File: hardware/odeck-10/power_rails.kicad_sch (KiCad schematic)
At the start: 0 parts

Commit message: Draft power sheets (input, laptop output, rails) and BOM stock audit
- power_input: TPS26750/TPD4S480 EPR sink, LM74800 PD-in and barrel paths
  (reverse/OV/UV), hardware PD-in priority, EXT_PWR_PRESENT, INA237 VIN monitor
- power_laptop: LM51770 buck-boost 5-28 V x 5 A with VSEL-only voltage steps,
  gated source switch, interlocked bus-power sink, latched 30.8 V OVP, INA226
- power_rails: LM5148 5 V/8 A with ideal-diode backfeed blocking, TPS62933
  3.3 V and 1.15 V, INA226
- tools/bom_check.py: JLC-stock-only audit (>=5); all 116 parts pass
- schgen fixes: multi-line notes, PWR_FLAG skipped in verify, import --force
- docs: design notes per sheet, I2C map, cross-sheet integration items

Co-Authored-By: Claude Opus 5.5 <noreply@anthropic.com>
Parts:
- added C301: 47u/100V, Capacitor_SMD:CP_Elec_10x10, symbol Device:C_Polarized
- added C302, C303, C304, C305: 4.7u/100V, Capacitor_SMD:C_1210_3225Metric, symbol Device:C
- added C306, C307: 100n/100V, Capacitor_SMD:C_0603_1608Metric, symbol Device:C
- added C308, C318, C323, C329, C331, C337, C338: 100n, Capacitor_SMD:C_0402_1005Metric, symbol Device:C
- added C309: 1n/100V, Capacitor_SMD:C_0603_1608Metric, symbol Device:C
- added C310, C311, C312, C313, C314, C315: 47u/10V, Capacitor_SMD:C_1210_3225Metric, symbol Device:C
- added C316: 1u/100V, Capacitor_SMD:C_0805_2012Metric, symbol Device:C
- added C317: 4.7u, Capacitor_SMD:C_0603_1608Metric, symbol Device:C
- added C319: 10n, Capacitor_SMD:C_0402_1005Metric, symbol Device:C
- added C320: 100p, Capacitor_SMD:C_0402_1005Metric, symbol Device:C
- added C321, C322: 100n/50V, Capacitor_SMD:C_0603_1608Metric, symbol Device:C
- added C324: 330u/6.3V, Capacitor_SMD:CP_Elec_6.3x5.9, symbol Device:C_Polarized
- added C325, C326, C332, C333, C334: 22u, Capacitor_SMD:C_0805_2012Metric, symbol Device:C
- added C327, C328, C335, C336: 10u, Capacitor_SMD:C_0805_2012Metric, symbol Device:C
- added C330: 22n, Capacitor_SMD:C_0402_1005Metric, symbol Device:C
- added C339, C340, C341, C342: 22u, Capacitor_SMD:C_0603_1608Metric, symbol Device:C
- added D301: BAT46W, Diode_SMD:D_SOD-123, symbol Device:D_Schottky
- added L301: 4.7u, odeck:IND-SMD_L13.45-W12.6, symbol odeck:MWSA1206S-4R7MT
- added L302: 2.2u, odeck:IND-SMD_L5.4-W5.2, symbol odeck:MWSA0503S-2R2MT
- added L303: 1.5u, odeck:IND-SMD_L5.4-W5.2, symbol odeck:MWSA0503S-1R5MT
- added Q301: BSZ070N08LS5, odeck:PG-TSDSON-8_L3.3-W3.3-P0.65-BL-1, symbol odeck:BSZ070N08LS5
- added Q302: BSC0805LS, odeck:PG-TDSON-8_L5.2-W5.9-P1.27-LS6.2-BL-EP, symbol odeck:BSC0805LS
- added Q303: BSC0901NS, odeck:DFN-8_L5.9-W5.2-P1.27-LS6.2-BL, symbol odeck:BSC0901NS
- added R301: 0, Resistor_SMD:R_0402_1005Metric, symbol Device:R
- added R302: 2.2, Resistor_SMD:R_0805_2012Metric, symbol Device:R
- added R303: 4m, Resistor_SMD:R_2512_6332Metric, symbol Device:R
- added R304: 100k, Resistor_SMD:R_0805_2012Metric, symbol Device:R
- added R305: 14.3k, Resistor_SMD:R_0402_1005Metric, symbol Device:R
- added R306: 73.2k, Resistor_SMD:R_0402_1005Metric, symbol Device:R
- added R307: 41.2k, Resistor_SMD:R_0402_1005Metric, symbol Device:R
- added R308: 64.9k, Resistor_SMD:R_0402_1005Metric, symbol Device:R
- added R309, R317: 12k, Resistor_SMD:R_0402_1005Metric, symbol Device:R
- added R310, R316, R318, R321: 10k, Resistor_SMD:R_0402_1005Metric, symbol Device:R
- added R311, R313, R319: 100k, Resistor_SMD:R_0402_1005Metric, symbol Device:R
- added R312: 2m, Resistor_SMD:R_2512_6332Metric, symbol Device:R
- added R314: 39k, Resistor_SMD:R_0402_1005Metric, symbol Device:R
- added R315: 31.6k, Resistor_SMD:R_0402_1005Metric, symbol Device:R
- added R320: 4.42k, Resistor_SMD:R_0402_1005Metric, symbol Device:R
- added U301: LM5148, odeck:VQFN-24_L5.5-W3.5-P0.50-BL-EP-2, symbol odeck:LM5148RGYR
- added U302: LM74700-Q1, odeck:SOT-23-6_L2.9-W1.6-P0.95-LS2.8-TL, symbol odeck:LM74700QDBVTQ1
- added U303: INA226, odeck:MSOP-10_L3.0-W3.0-P0.50-LS5.0-BL, symbol odeck:INA226AIDGSR
- added U304: TPS62933, odeck:SOT-583-8_L2.1-W1.2-P0.50-LS1.6-BR, symbol odeck:TPS62933DRLR
- added U305: TPS62933P, odeck:SOT-583-8_L2.1-W1.2-P0.50-LS1.6-BL, symbol odeck:TPS62933PDRLR
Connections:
- new net +1V15: C339.1, C340.1, C341.1, C342.1, L303.2, R320.1
- new net +3V3: C323.1, C332.1, C333.1, C334.1, L302.2, R315.1, R317.1, R319.2, U303.2 (A0), U303.6 (VS+)
- new net +5V: C324.1, C325.1, C326.1, C327.1, C328.1, C329.1, C335.1, C336.1, C337.1, R312.2, R313.1, U303.8 (VBUS), U303.9 (VIN-), U304.3 (VIN), U305.3 (VIN)
- new net 1V15_BST: C338.1, U305.6 (BST)
- new net 1V15_EN: R317.2, R318.1, U305.2 (EN)
- new net 1V15_FB: R320.2, R321.1, U305.8 (FB)
- new net 1V15_SW: C338.2, L303.1, U305.5 (SW)
- new net 3V3_BST: C331.1, U304.6 (BST)
- new net 3V3_EN: R313.2, R314.1, U304.2 (EN)
- new net 3V3_FB: R315.2, R316.1, U304.8 (FB)
- new net 3V3_SS: C330.1, U304.7 (SS)
- new net 3V3_SW: C331.2, L302.1, U304.5 (SW)
- new net 5V_BOOT: C308.1, U301.15 (CBOOT)
- new net 5V_BUCK: C310.1, C311.1, C312.1, C313.1, C314.1, C315.1, C321.2, Q303.1 (S), Q303.2 (S), Q303.3 (S), R303.2, R308.1, R311.1, U301.16 (VCCX), U301.21 (VOUT), U302.3 (EN), U302.6 (ANODE)
- new net 5V_CC: C319.1, R310.2
- new net 5V_CNFG: R307.1, U301.3 (CNFG)
- new net 5V_COMP: C320.1, R310.1, U301.5 (EXTCOMP)
- new net 5V_EN: R304.2, R305.1, U301.19 (EN)
- new net 5V_FB: R308.2, R309.1, U301.6 (FB)
- new net 5V_HG: Q301.4 (G), R301.2
- new net 5V_HO: R301.1, U301.13 (HO)
- new net 5V_ISNS: L301.2, R303.1, U301.20 (ISNS+)
- new net 5V_LG: Q302.4 (G), U301.11 (LO)
- new net 5V_OR: C322.1, Q303.5 (D), Q303.6 (D), Q303.7 (D), Q303.8 (D), Q303.9 (D), R312.1, U302.4 (CATHODE), U303.10 (VIN+)
- new net 5V_ORG: Q303.4 (G), U302.5 (GATE)
- new net 5V_RT: R306.1, U301.4 (RT)
- new net 5V_SNB: C309.1, R302.2
- new net 5V_SW: C308.2, L301.1, Q301.1 (S), Q301.2 (S), Q301.3 (S), Q302.5 (D), Q302.6 (D), Q302.7 (D), Q302.8 (D), Q302.9 (EP), R302.1, U301.14 (SW)
- new net 5V_VCAP: C321.1, U302.1 (VCAP)
- new net 5V_VCC: C317.1, U301.9 (VCC)
- new net 5V_VDDA: C318.1, U301.18 (PFM/SYNC), U301.8 (VDDA)
- new net 5V_VINC: C316.1, D301.1 (K), U301.12 (VIN)
- new net GND: C301.2, C302.2, C303.2, C304.2, C305.2, C306.2, C307.2, C309.2, C310.2, C311.2, C312.2, C313.2, C314.2, C315.2, C316.2, C317.2, C318.2, C319.2, C320.2, C322.2, C323.2, C324.2, C325.2, C326.2, C327.2, C328.2, C329.2, C330.2, C332.2, C333.2, C334.2, C335.2, C336.2, C337.2, C339.2, C340.2, C341.2, C342.2, Q302.1 (S), Q302.2 (S), Q302.3 (S), R305.2, R306.2, R307.2, R309.2, R314.2, R316.2, R318.2, R321.2, U301.1 (NC), U301.10 (PGND), U301.2 (NC), U301.22 (NC), U301.23 (NC), U301.24 (NC), U301.25 (EP), U301.7 (AGND), U302.2 (GND), U303.1 (A1), U303.7 (GND), U304.1 (RT), U304.4 (GND), U305.1 (RT), U305.4 (GND)
- new net I2C_SYS_SCL: U303.5 (SCL)
- new net I2C_SYS_SDA: U303.4 (SDA)
- new net PG_5V: R311.2, U301.17 (PG/SYNCOUT)
- new net RAILS_PG: R319.1, U305.7 (PG)
- new net VIN: C301.1, C302.1, C303.1, C304.1, C305.1, C306.1, C307.1, D301.2 (A), Q301.5 (D), Q301.6 (D), Q301.7 (D), Q301.8 (D), R304.1
- no-connect marks 0 -> 1
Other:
- note added: "+1V1: not needed. RP2350 core (DVDD 1.1 V) comes from its internal switching regulator (VREG_VIN from +3V3)."
- note added: "+5V rises 5.0 -> 5.11 V, EXT_PWR_PRESENT opens the sink switch. Loss of VIN: +5V held by 330 uF + ceramics."
- note added: "-> place a dedicated 0.95 V buck (e.g. TLV62569 from +3V3, EN = POW_EXT_SWR) on the ethernet sheet."
- note added: "1. +5V MAIN BUCK LM5148 (80 V sync buck controller) VIN 9-50 V -> 5V_BUCK = 5.13 V, 8 A, fsw 300 kHz"
- note added: "2. BACKFEED BLOCK 5V_BUCK -> ideal diode (LM74700 + BSC0901NS) -> 5V_OR -> 2 mOhm shunt -> +5V"
- note added: "3. +3V3 TPS62933 (3.8-30 V in, 3 A) +5V -> 3.33 V, 1.2 MHz"
- note added: "4. +1V15 USB7206C VCORE (1.09-1.21 V, 1.15 V nom.) TPS62933P +5V -> 1.154 V, 1.2 MHz"
- note added: "5. RAILS NOT CREATED HERE"
- note added: "A plain sync buck would conduct +5V -> L -> Q301 body diode -> VIN (~4.3 V on VIN, which would also wake the"
- note added: "ALERT unused (firmware polls); I2C pull-ups live on the MCU sheet."
- note added: "Buck running: Q303 regulated to 20 mV forward drop (0.16 W at 8 A); reverse current -> gate pulled in <0.75 us."
- note added: "Comp (gm 1.2 mS, Gcs 10): RCOMP 10k, CCOMP 10n (zero 1.6 kHz), CHF 100p (pole 159 kHz)."
- note added: "EN divider 100k/39k: starts at +5V > 4.31 V (stops ~4.0 V) so a sagging bus-powered +5V cannot half-start the rail."
- note added: "FIX: the buck regulates its own node 5V_BUCK; LM74700 + Q303 form an ideal diode 5V_BUCK -> +5V."
- note added: "GL3224: single 5 V supply (4.75-5.25 V) on its VBUS pin, internal 3.3 V / 1.2 V regulators -> fed from +5V."
- note added: "Handover: external power arrives -> buck soft-starts (3 ms) into 5V_BUCK -> diode conducts once 5V_BUCK > +5V,"
- note added: "INA226 @ 0x41 (A1=GND, A0=VS): 2 mOhm, 8 A = 16 mV of +-81.92 mV FS; CURRENT_LSB 0.5 mA -> CAL = 5120."
- note added: "L = 4.7 uH: dI = 3.25 A p-p at 48 V, 2.7 A at 20 V. Slope comp: L_ideal = Vo*Rs/(24*f) = 2.85 uH -> 1.65x (stable)."
- note added: "LM51770 buck-boost at its 3.5 V UVLO and the LM5148's VOUT->VIN ESD diode would conduct too)."
- note added: "LOCAL NET - intended to be wire-ORed onto HUB_RESET_N (hold hub in reset until VCORE is good). See docs."
- note added: "Load ~1.5 A typ / 2.2 A max (hub VDD33, RTL8156BG, muxes, PMG1, RP2350, LCD, SD cards): ~0.3-0.7 W loss."
- note added: "Loss at 8 A: ~2.6 W (20 V in, 94 %), ~3.6 W (48 V in, 92 %); incl. OR-FET + INA shunt: 93.3 % / 91.4 %."
- note added: "Measures buck output only; bus-powered +5V current is seen by the laptop-VBUS INA226 (power_laptop)."
- note added: "Nothing on this sheet ties VIN-side pins to +5V (FB, VCCX, VOUT/ISNS+, PG pull-up all on 5V_BUCK)."
- note added: "PFM/SYNC = VDDA: diode emulation, no negative inductor current (cannot pump +5V energy back into VIN)."
- note added: "PROBLEM: in bus-powered mode +5V is fed from laptop VBUS (sink switch, power_laptop sheet) while VIN is absent."
- note added: "RAILS_PG (open drain, 100k to +3V3): high only when +1V15 is in regulation, which implies +3V3 is up."
- note added: "RTL8156BG (non-S) has NO internal regulator: it needs an external 0.95 V (0.92-0.98 V, <= 650 mA) buck that it"
- note added: "Rs = 4 mOhm, VCS-TH 49/60/73 mV -> peak limit 12.3/15/18.3 A, DC >= 10.6 A at 48 V; short-circuit peak 18.7 A < 24 A Isat."
- note added: "Sequencing (sec. 9.6.1): VCORE rises after or with VDD33 -> EN from +3V3 divider; rise times <= 5 ms -> fixed 2 ms SS."
- note added: "Sequencing: hub needs VCORE >= after VDD33 (done here); RTL8156BG sequences its own 0.95 V; GL3224 needs none."
- note added: "Soft start 3.2 ms (3.9 ms worst): inside RTL8156BG 3.3 V rise 0.5-10 ms and USB7206C <= 5 ms."
- note added: "USB7206C (DS00003850F): VCORE 1.09-1.21 V; ~1.31 A with all 5 ports at 10G (410 mA + 179 mA/port). 1.154 V +-1.5 % -> 1.137-1.171 V."
- note added: "VCCX = own output (> 4.3 V): gate drive from 5 V instead of the VIN LDO (saves ~0.5 W at 48 V)."
- note added: "VIN absent: LM74700 unpowered (ANODE ~0 V), Q303 off, its body diode reverse-biased -> zero reverse current."
- note added: "VIN at a few volts: EN/UVLO divider keeps the LM5148 off below 7.0-8.0 V, D301 isolates its VIN pin."
- note added: "dI = 1.15*(1-1.15/5.13)/(1.5u*1.2M) = 0.50 A p-p (17 % of 3 A, >10 % min for PCM). Cout 4x22 uF (+ hub 9x4.7 uF)."
- note added: "dI = 3.33*(1-3.33/5.13)/(2.2u*1.2M) = 0.44 A p-p (15 % of 3 A). Cout 3x22 uF (~35 uF eff. at 3.3 V; TI table: 30 uF typ, 10 uF min)."
- note added: "enables itself via pin 5 POW_EXT_SWR (rise 0.5-2.2 ms). Only the RTL8156BGS has REG_OUT, and it is not stocked."
- note added: "fc = 18 kHz with ~430 uF total (+5V bulk + ceramics); 52 kHz with buck-side ceramics only (~150 uF) - both < fsw/5."
- note added: "fsw = 1e6/(45*73.2k+53) = 299 kHz; tON at 50.4 V = 340 ns >> 50 ns min; dropout below ~5.3 V (VIN UVLO is 8 V)."
- note removed: "TODO — planned contents: LM5148 5V/8A buck, 3.3V (TPS62933/TPS563201), 1.15V/2A hub core, 1.2V/1.1V as needed, INA226 on 5V rail + laptop VBUS, INA228/INA238 on VIN (85V)."
- title: odeck-10 — Rails -> odeck-10 — Power rails (+5V / +3V3 / +1V15)

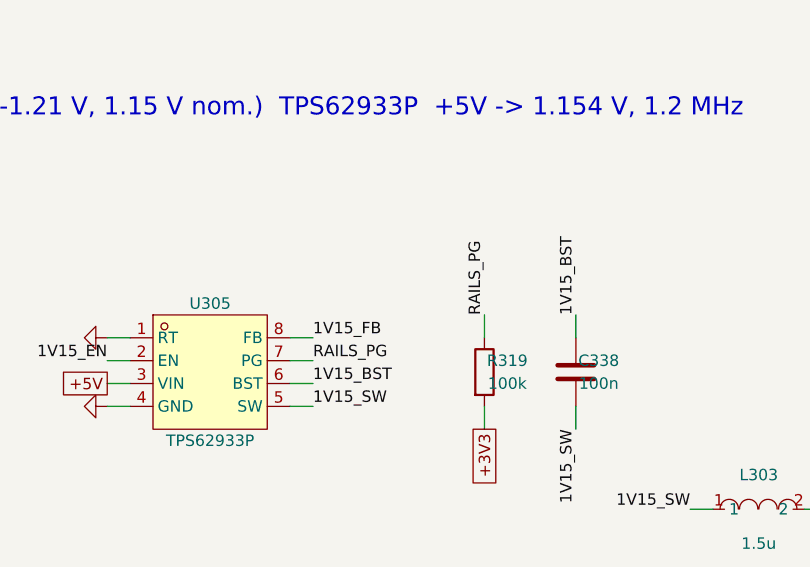
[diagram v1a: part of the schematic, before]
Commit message: Draft data-path sheets: PD controller, USB-C muxes/DP, USB hub
- pd_pmg1: PMG1-S3 (CYPM1321, dead-battery Rd) dual-port: laptop EPR source +
  DP UFP_D, downstream 5 V/3 A + DP DFP_D, HPD relay, VBUS-powered cold start,
  I2C 0x42, SWD/reset via cuttable jumpers
- usbc_muxes: laptop + downstream USB-C, TUSB1064/TUSB1046 in GPIO mode,
  TPD4S480 (EPR) / TPD6S300 CC protection, 10G-rated ESD, AC coupling
- usb_hub: USB7206C port map, SMBus-optional boot, reset gated by RAILS_PG,
  BC1.2 on USB-A ports, hub-TX AC caps
- schgen: in_bom option; nets: VBUS_LSW, PMG1_VDDD, hub/mux/CC links
- import_lcsc.sh: guard against overwriting other parts' footprints
- 137 parts, all JLC stock >= 5

Co-Authored-By: Claude Opus 5.5 <noreply@anthropic.com>
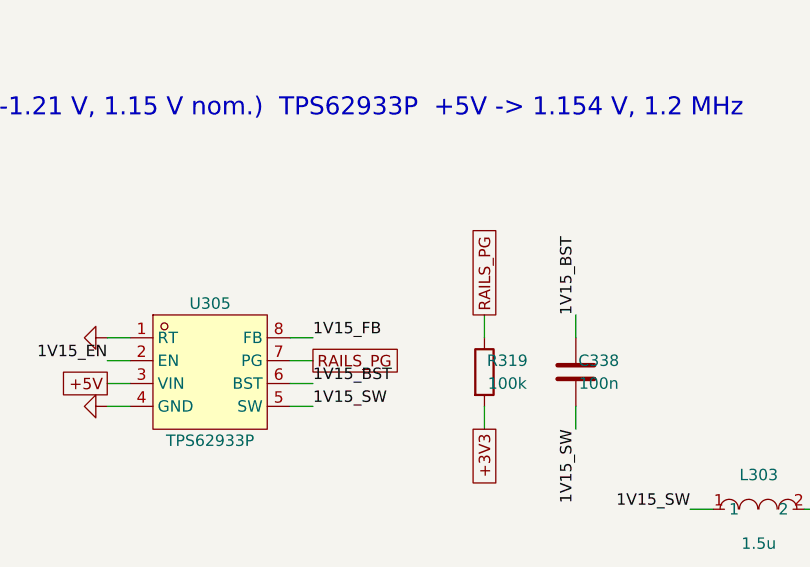
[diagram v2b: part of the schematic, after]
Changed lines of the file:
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@@
 		)
 	)
-	(label "RAILS_PG"
+	(global_label "RAILS_PG"
+		(shape passive)
 		(at 422.91 161.29 0)
+		(fields_autoplaced yes)
 		(effects
 			(font
 				(size 1.27 1.27)
 			)
-			(justify left bottom)
+			(justify left)
+		)
+		(property "Intersheetrefs" "${INTERSHEET_REFS}"
+			(at 422.91 161.29 0)
+			(effects
+				(font
+					(size 1.27 1.27)
+				)
+				(hide yes)
+			)
 		)
 	)
@@
 		)
 	)
-	(label "RAILS_PG"
+	(global_label "RAILS_PG"
+		(shape passive)
 		(at 441.96 156.21 90)
+		(fields_autoplaced yes)
 		(effects
 			(font
 				(size 1.27 1.27)
 			)
-			(justify left bottom)
+			(justify left)
+		)
+		(property "Intersheetrefs" "${INTERSHEET_REFS}"
+			(at 441.96 156.21 0)
+			(effects
+				(font
+					(size 1.27 1.27)
+				)
+				(hide yes)
+			)
 		)
 	)

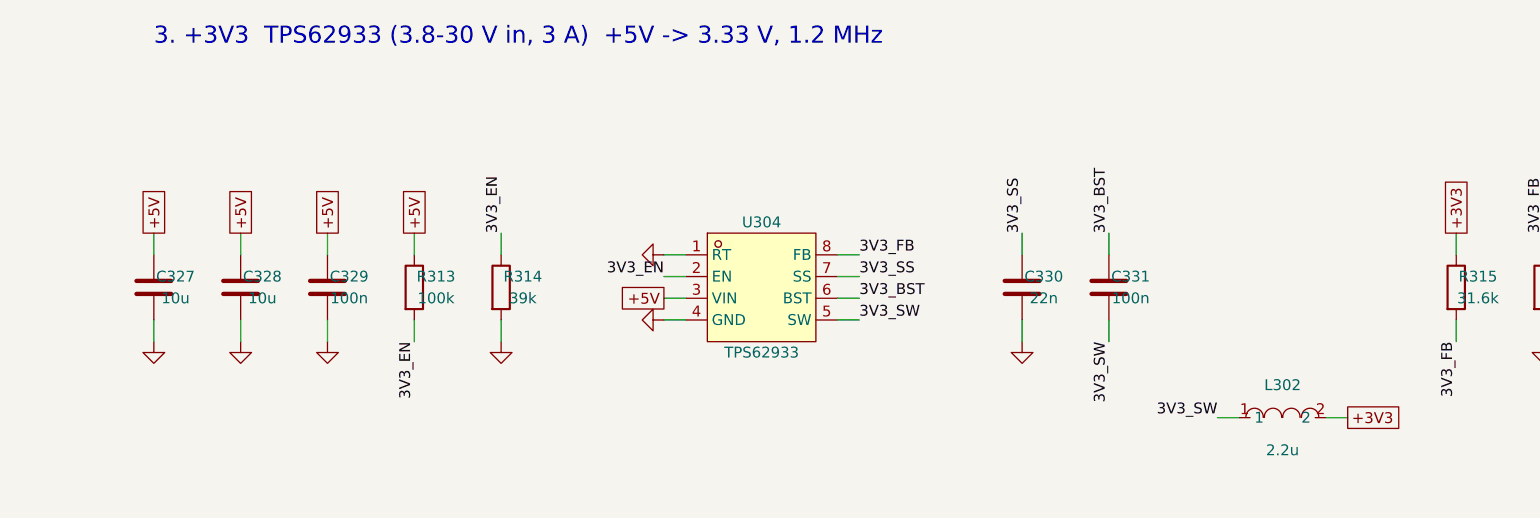
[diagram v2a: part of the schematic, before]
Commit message: Draft remaining sheets: USB-A, card reader, Ethernet, MCU, display/UI, sensors
- usb_a: 2x 10G USB-A, TPS2553 switches (hub OR RP2350 force), INA180 sense
- card_reader: GL3224 + SD/microSD, card detect + activity to MCU
- ethernet: RTL8156BG with switched 3.3 V, 0.95 V PWM buck, 2.5G magjack,
  LED buffer, EUI-48 EEPROM + gated I2C bridge for MAC eFuse write
- mcu: RP2350B reference core, full GPIO table, TCA9534 expander, PIO I2C
- display_ui: 2.0" ST7789 LCD + backlight PWM, buttons, unpopulated GPIO
  header (series R + ESD), Qwiic
- sensors: 8x TMP1075, 2 NTCs, thermocouple pads
- integration: ETH_I2C_EN net, TPS62933F for +3V3, PWR_FLAGs
- schgen: deterministic UUIDs; bom_check: cost summary
- 181 parts, all JLC stock >= 5; netlist verify OK; ERC clean but 1 spare pin

Co-Authored-By: Claude Opus 5.5 <noreply@anthropic.com>
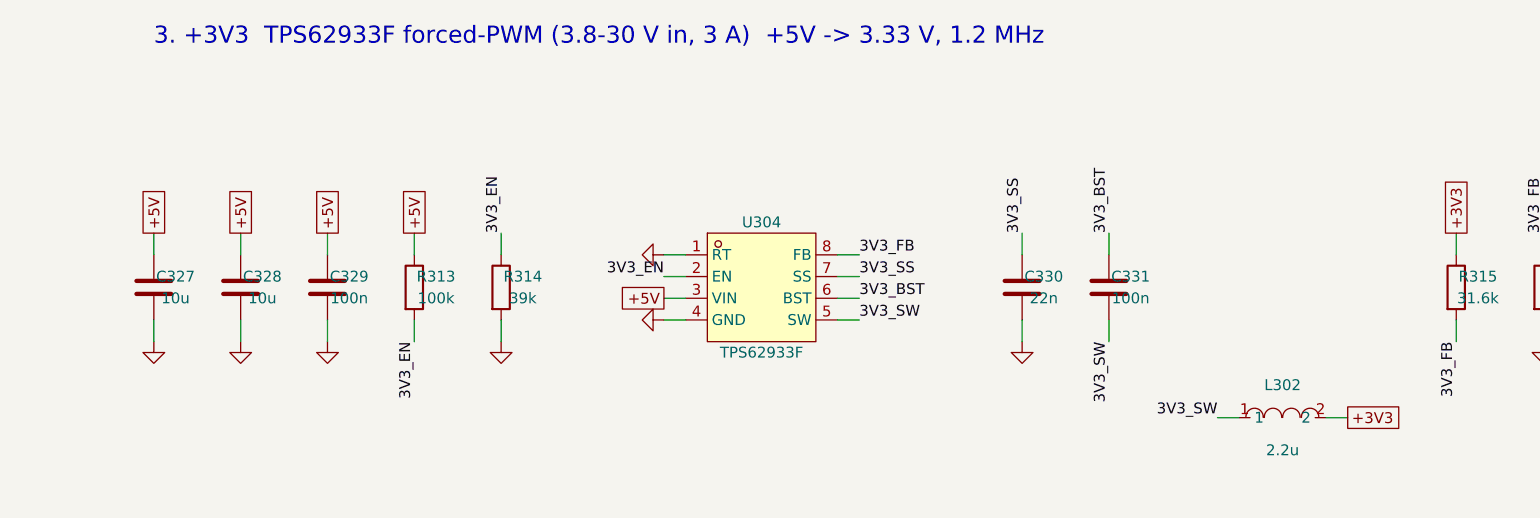
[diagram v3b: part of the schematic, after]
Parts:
- U304: value TPS62933 -> TPS62933F; LCSC C3200405 -> C5219272; MPN TPS62933DRLR -> TPS62933FDRLR
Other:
- note added: "3. +3V3 TPS62933F forced-PWM (3.8-30 V in, 3 A) +5V -> 3.33 V, 1.2 MHz"
- note removed: "3. +3V3 TPS62933 (3.8-30 V in, 3 A) +5V -> 3.33 V, 1.2 MHz"
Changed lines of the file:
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@@
 			)
 		)
-		(property "Value" "TPS62933"
+		(property "Value" "TPS62933F"
 			(at 411.48 60.96 0)
 			(effects
@@
 			)
 		)
-		(property "Description" "3 A sync buck, RT=GND -> 1.2 MHz"
+		(property "Description" "3 A sync buck, forced PWM (RTL8156BG needs >=1 MHz PWM supply), RT=GND -> 1.2 MHz; same pinout as TPS62933"
 			(at 411.48 53.34 0)
 			(effects
@@
 			)
 		)
-		(property "LCSC" "C3200405"
+		(property "LCSC" "C5219272"
 			(at 411.48 53.34 0)
 			(effects
@@
 			)
 		)
-		(property "MPN" "TPS62933DRLR"
+		(property "MPN" "TPS62933FDRLR"
 			(at 411.48 53.34 0)
 			(effects
@@
 		)
 	)
-	(text "3. +3V3  TPS62933 (3.8-30 V in, 3 A)  +5V -> 3.33 V, 1.2 MHz"
+	(text "3. +3V3  TPS62933F forced-PWM (3.8-30 V in, 3 A)  +5V -> 3.33 V, 1.2 MHz"
 		(exclude_from_sim no)
 		(at 340.36 22.86 0)

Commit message: Schematic review + footprint verification; fix all MAJOR findings
Reviews (docs/review/): power, PD/mux, data path, MCU/UI - 0 blockers,
7 majors, all resolved:
- power: diode-OR inputs (no shutdown-based PD-in priority), sink hand-over
  gated by delayed PG_5V, PD-in capacitance within 100 uF, HV resistor sizes,
  OVP filter/threshold, VBB_PG soft-start qualification
- card reader MS2_INS/SD2_WP phantom card, hub VBUS_DET level buffer
- RP2350 inductor dot text; minors across all sheets (HPD pull-down, PMG1
  INT pin, PHY TX caps, erratum E9 pull-downs, PHY I2C bridge gating,
  backlight 39 ohm, +1V1 cap, IOX P7)
Footprints: all 54 custom footprints checked vs manufacturer drawings,
50 fixed (courtyards, pads, paste, RJ45 mirrored pinout, EP sizes, holes);
removed obsolete FL_001 placeholder.
Firmware rules collected in docs/design/mcu.md.
186 parts, all JLC stock >= 5; netlist verify OK; ERC clean.

Co-Authored-By: Claude Opus 5.5 <noreply@anthropic.com>
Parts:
- removed C342: 22u, Capacitor_SMD:C_0603_1608Metric, symbol Device:C
- C301: value 47u/100V -> 4.7u/100V; footprint Capacitor_SMD:CP_Elec_10x10 -> Capacitor_SMD:C_1210_3225Metric; symbol Device:C_Polarized -> Device:C; LCSC C371305 -> C697607
- C305: value 4.7u/100V -> 100n/100V; footprint Capacitor_SMD:C_1210_3225Metric -> Capacitor_SMD:C_0603_1608Metric; LCSC C697607 -> C15725
- C307: value 100n/100V -> 100n; footprint Capacitor_SMD:C_0603_1608Metric -> Capacitor_SMD:C_0402_1005Metric; LCSC C15725 -> C1525
- C308: value 100n -> 1n/100V; footprint Capacitor_SMD:C_0402_1005Metric -> Capacitor_SMD:C_0603_1608Metric; LCSC C1525 -> C106247; now not fitted
- C309: value 1n/100V -> 47u/10V; footprint Capacitor_SMD:C_0603_1608Metric -> Capacitor_SMD:C_1210_3225Metric; LCSC C106247 -> C84494; now fitted
- C315: value 47u/10V -> 1u/100V; footprint Capacitor_SMD:C_1210_3225Metric -> Capacitor_SMD:C_0805_2012Metric; LCSC C84494 -> C126585
- C316: value 1u/100V -> 4.7u; footprint Capacitor_SMD:C_0805_2012Metric -> Capacitor_SMD:C_0603_1608Metric; LCSC C126585 -> C19666
- C317: value 4.7u -> 100n; footprint Capacitor_SMD:C_0603_1608Metric -> Capacitor_SMD:C_0402_1005Metric; LCSC C19666 -> C1525
- C318: value 100n -> 10n; LCSC C1525 -> C15195
- C319: value 10n -> 100p; LCSC C15195 -> C1546
- C320: value 100p -> 100n/50V; footprint Capacitor_SMD:C_0402_1005Metric -> Capacitor_SMD:C_0603_1608Metric; LCSC C1546 -> C14663
- C322: value 100n/50V -> 100n; footprint Capacitor_SMD:C_0603_1608Metric -> Capacitor_SMD:C_0402_1005Metric; LCSC C14663 -> C1525
- C323: value 100n -> 330u/6.3V; footprint Capacitor_SMD:C_0402_1005Metric -> Capacitor_SMD:CP_Elec_6.3x5.9; symbol Device:C -> Device:C_Polarized; LCSC C1525 -> C54321566
- C324: value 330u/6.3V -> 22u; footprint Capacitor_SMD:CP_Elec_6.3x5.9 -> Capacitor_SMD:C_0805_2012Metric; symbol Device:C_Polarized -> Device:C; LCSC C54321566 -> C45783
- C326, C334: value 22u -> 10u; LCSC C45783 -> C15850
- C328, C336: value 10u -> 100n; footprint Capacitor_SMD:C_0805_2012Metric -> Capacitor_SMD:C_0402_1005Metric; LCSC C15850 -> C1525
- C329: value 100n -> 22n; LCSC C1525 -> C1532
- C330: value 22n -> 100n; LCSC C1532 -> C1525
- C331: value 100n -> 22u; footprint Capacitor_SMD:C_0402_1005Metric -> Capacitor_SMD:C_0805_2012Metric; LCSC C1525 -> C45783
- C338: value 100n -> 22u; footprint Capacitor_SMD:C_0402_1005Metric -> Capacitor_SMD:C_0603_1608Metric; LCSC C1525 -> C59461
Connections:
- net +1V15: now also C338.1
- net +3V3: now also C322.1, C331.1; no longer C323.1, C334.1
- net +5V: now also C323.1, C334.1; no longer C329.1, C337.1
- net 1V15_BST: now also C337.1; no longer C338.1
- net 1V15_SW: now also C337.2; no longer C338.2
- net 3V3_BST: now also C330.1; no longer C331.1
- net 3V3_SS: now also C329.1; no longer C330.1
- net 3V3_SW: now also C330.2; no longer C331.2
- net 5V_BOOT: now also C307.1; no longer C308.1
- net 5V_BUCK: now also C309.1, C320.2; no longer C315.1, C321.2
- net 5V_CC: now also C318.1; no longer C319.1
- net 5V_COMP: now also C319.1; no longer C320.1
- net 5V_OR: now also C321.1; no longer C322.1
- net 5V_SNB: now also C308.1; no longer C309.1
- net 5V_SW: now also C307.2; no longer C308.2
- net 5V_VCAP: now also C320.1; no longer C321.1
- net 5V_VCC: now also C316.1; no longer C317.1
- net 5V_VDDA: now also C317.1; no longer C318.1
- net 5V_VINC: now also C315.1; no longer C316.1
- net GND: now also C308.2, C321.2, C331.2, C338.2; no longer C307.2, C320.2, C330.2, C337.2
- net VIN: no longer C307.1
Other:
- note added: "+5V rises 5.0 -> 5.11 V; PG_5V (global, open drain, 100k to 5V_BUCK = 5.1 V level) goes high and, after a"
- note added: "2.7-6.7 ms RC on power_laptop, opens the sink switch (EXT_PWR_PRESENT AND PG_5V). Make-before-break."
- note added: "GLOBAL NET (nets.py): wire-ORed onto HUB_RESET_N on usb_hub through a Schottky (hub held in reset until VCORE good)."
- note added: "Loss of VIN: +5V held by 330 uF + ceramics."
- note added: "PG floating) and would read 'good' exactly in the hand-over window. Do not feed PG_5V to 3.3 V-only inputs."
- note added: "PG_5V pull-up is deliberately 5V_BUCK, not +3V3/+5V: those exist while the LM5148 is unpowered (open-drain"
- note removed: "+5V rises 5.0 -> 5.11 V, EXT_PWR_PRESENT opens the sink switch. Loss of VIN: +5V held by 330 uF + ceramics."
- note removed: "LOCAL NET - intended to be wire-ORed onto HUB_RESET_N (hold hub in reset until VCORE is good). See docs."
- moved on the sheet: C302, C303, C304, C305, C306, C307, C310, C311, C312, C313, C314, C315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

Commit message: Cost pass, PCB sync + rough placement, renders, README
- cost pass: extended parts 129 -> 114 (~$45/order less), nets unchanged
- tools/pcbsync.py: scripted update-PCB-from-schematic (keeps placed parts)
- tools/set_outline.py; board grown to 130x85 mm (provisional)
- hardware/odeck-10/placement.py: edge connectors + anchor-based packing,
  small passives spill to bottom; all 796 parts on the board (2 at anchor)
- docs/images: top/bottom/iso renders of the rough placement
- README.md: overview, architecture, repo layout, workflow, roadmap

Co-Authored-By: Claude Opus 5.5 <noreply@anthropic.com>
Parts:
- C305, C306: footprint Capacitor_SMD:C_0603_1608Metric -> Capacitor_SMD:C_0805_2012Metric; LCSC C15725 -> C28233
- R304: LCSC C96346 -> C149504
- R314: footprint Resistor_SMD:R_0402_1005Metric -> Resistor_SMD:R_0603_1608Metric; LCSC C25783 -> C23153
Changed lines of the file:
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@@
 			)
 		)
-		(property "Footprint" "Capacitor_SMD:C_0603_1608Metric"
+		(property "Footprint" "Capacitor_SMD:C_0805_2012Metric"
 			(at 88.90 50.80 0)
 			(effects
@@
 			)
 		)
-		(property "LCSC" "C15725"
+		(property "LCSC" "C28233"
 			(at 88.90 50.80 0)
 			(effects
@@
 			)
 		)
-		(property "Footprint" "Capacitor_SMD:C_0603_1608Metric"
+		(property "Footprint" "Capacitor_SMD:C_0805_2012Metric"
 			(at 101.60 50.80 0)
 			(effects
@@
 			)
 		)
-		(property "LCSC" "C15725"
+		(property "LCSC" "C28233"
 			(at 101.60 50.80 0)
 			(effects
@@
 			)
 		)
-		(property "LCSC" "C96346"
+		(property "LCSC" "C149504"
 			(at 58.42 195.58 0)
 			(effects
@@
 			)
 		)
-		(property "Footprint" "Resistor_SMD:R_0402_1005Metric"
+		(property "Footprint" "Resistor_SMD:R_0603_1608Metric"
 			(at 381.00 53.34 0)
 			(effects
@@
 			)
 		)
-		(property "LCSC" "C25783"
+		(property "LCSC" "C23153"
 			(at 381.00 53.34 0)
 			(effects
